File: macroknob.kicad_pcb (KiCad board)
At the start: 2 copper layers, 38.1 x 50.5 mm, 8 parts, among them SW1 RotaryEncoder_Switch, U1 Nice_Nano_V2

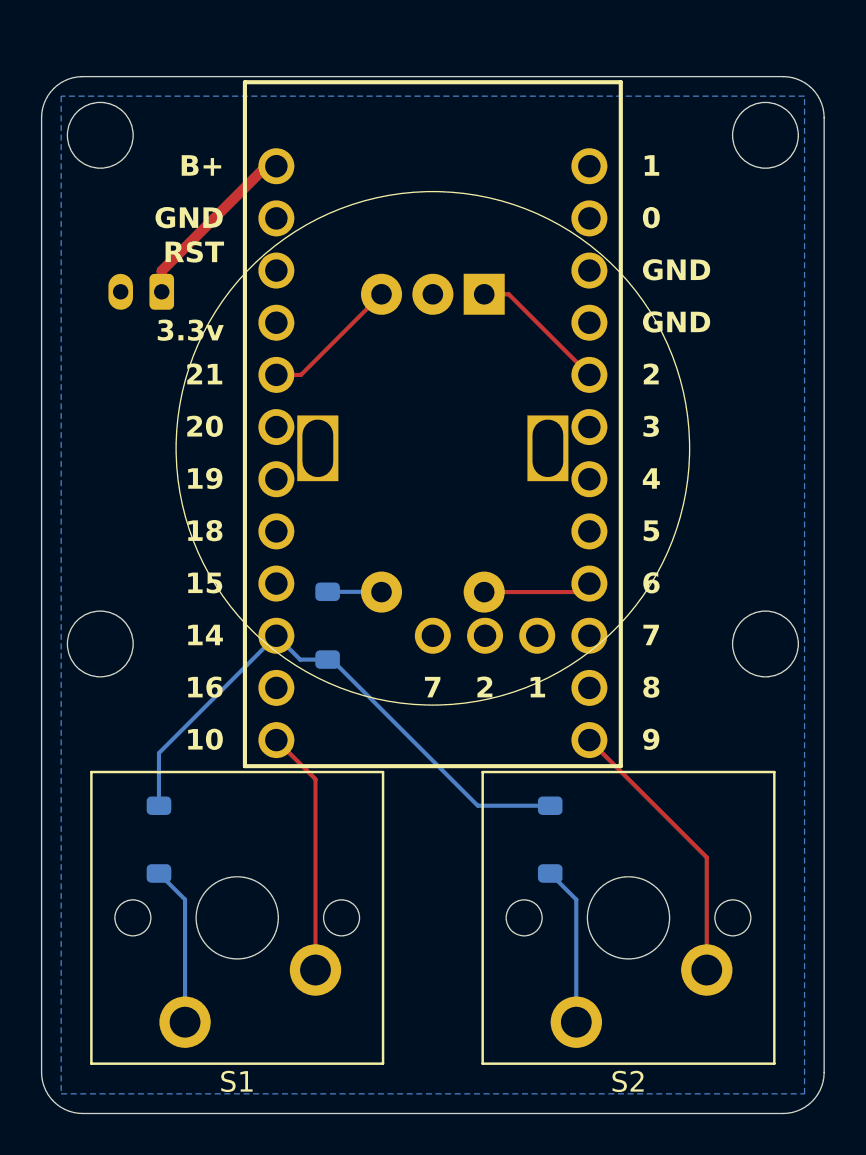
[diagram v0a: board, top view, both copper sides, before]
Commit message: Add V3 and case stl
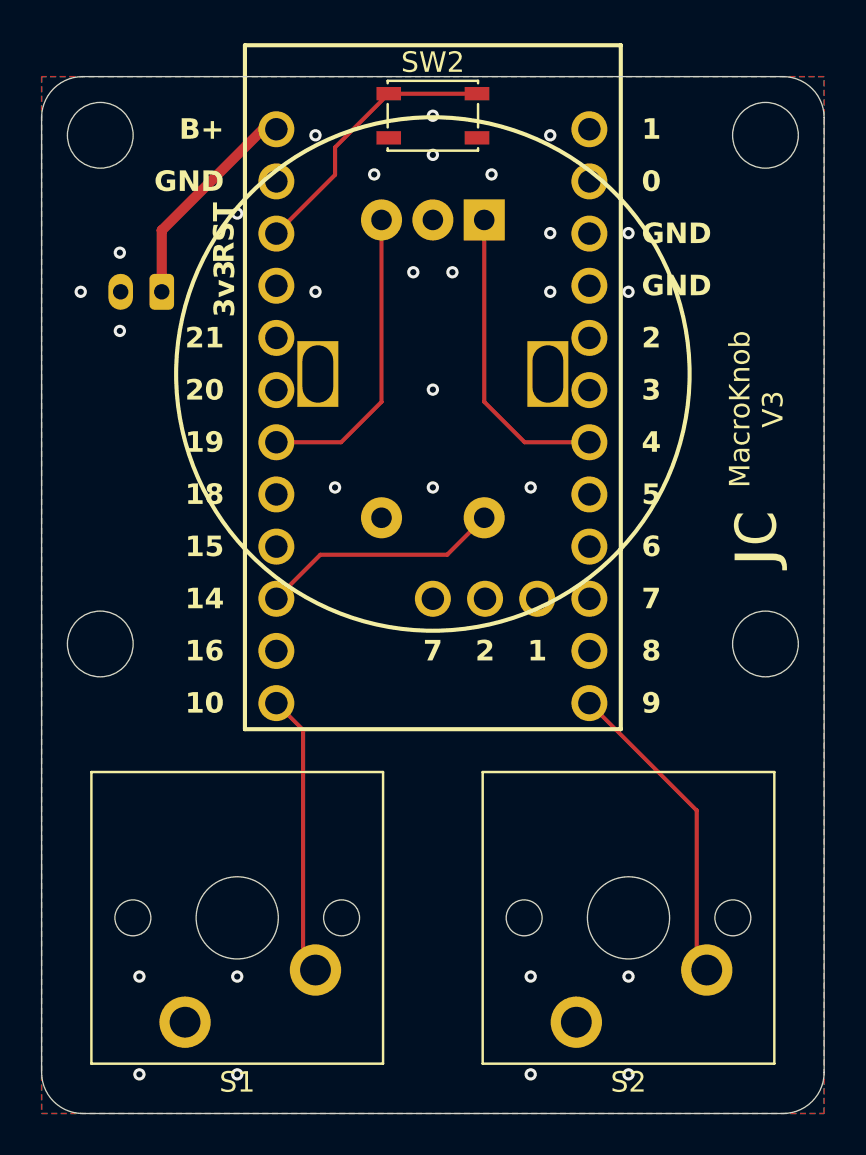
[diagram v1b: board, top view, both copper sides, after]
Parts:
- removed D1, D2, D3: Diode, ScottoKeebs_Components:Diode_SOD-123
- added SW2: Switch, Button_Switch_SMD:SW_SPST_PTS810, F.Cu at (114.9, 23.2)
- J1: renamed from + BAT -
- moved SW1 3.62 mm to (114.9, 35.8)
- moved U1 1.80 mm to (114.9, 37.5)
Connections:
- net Net-(J1-Pin_1) renamed B+
- net col1 renamed S1
- net col2 renamed S2
- S1 pad 2: Net-(D1-A) -> GND
- S2 pad 2: Net-(D2-A) -> GND
- SW1 pad A: rotB -> rotA
- SW1 pad B: rotA -> rotB
- SW1 pad S1: Net-(D3-A) -> GND
- SW1 pad S2: col3 -> S3
- U1 pad 15: row1 -> S3
- U1 pad 18: unconnected-(U1-19-Pad18) -> rotB
- U1 pad 20: rotA -> unconnected-(U1-21-Pad20)
- U1 pad 22: unconnected-(U1-RST-Pad22) -> Net-(U1-RST)
- U1 pad 5: rotB -> unconnected-(U1-2-Pad5)
- U1 pad 7: unconnected-(U1-4-Pad7) -> rotA
- U1 pad 9: col3 -> unconnected-(U1-6-Pad9)
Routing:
- net row1: track 27.4 -> 0.00 mm
- net Net-(U1-RST): track 0.00 -> 13.4 mm
- net S3: track 0.00 -> 11.8 mm
- net rotB: track 6.75 -> 14.8 mm
- net rotA: track 6.75 -> 14.8 mm
- net Net-(D1-A): track 7.77 -> 0.00 mm
- net Net-(D2-A): track 7.77 -> 0.00 mm
- net col3: track 5.29 -> 0.00 mm
- net Net-(D3-A): track 2.43 -> 0.00 mm
- net B+: track 8.71 -> 10.6 mm
- net S1: track 12.0 -> 13.8 mm
- net S2: track 13.6 -> 15.4 mm
- net GND: vias 0 -> 29
- added copper zone on F.Cu, net GND
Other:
- board text added: "C"
- board text added: "J"
- board text added: "MacroKnob V3"
